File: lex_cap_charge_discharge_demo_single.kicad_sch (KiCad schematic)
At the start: 12 parts, among them J1 +5V, J2 GND, SW1 charge, SW2 discharge

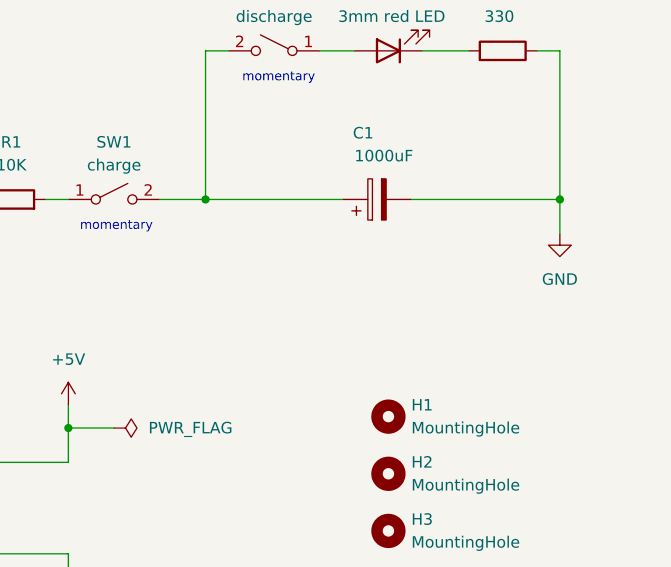
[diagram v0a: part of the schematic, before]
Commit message: Add optional component (with header) around cap
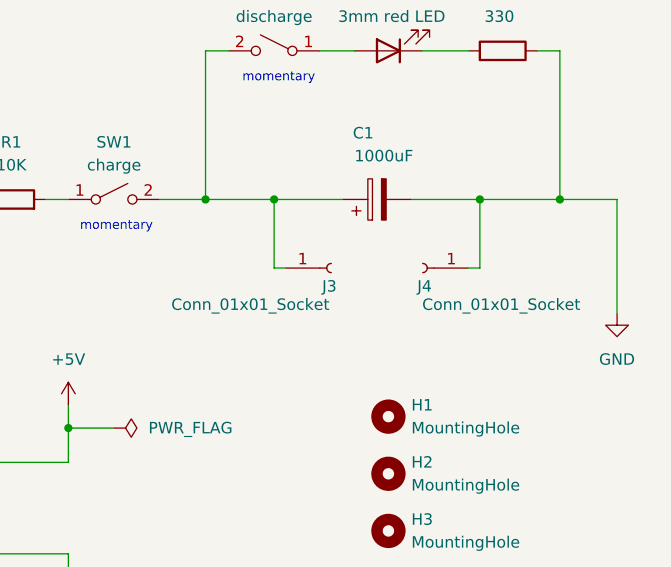
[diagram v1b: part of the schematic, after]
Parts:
- added J3, J4: Conn_01x01_Socket, Connector_PinSocket_2.54mm:PinSocket_1x01_P2.54mm_Vertical, symbol Connector:Conn_01x01_Socket
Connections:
- net GND: now also J4.1 (Pin_1)
- net at C1.1, SW1.2 (B), SW2.2 (B): now also J3.1 (Pin_1)
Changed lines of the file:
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@@
+	)
+	(junction
+		(at 167.64 44.45)
+		(diameter 0)
+		(color 0 0 0 0)
+	)
+	(junction
+		(at 144.78 44.45)
+		(diameter 0)
+		(color 0 0 0 0)
 	)
 	(junction
@@
 	(wire
 		(pts
-			(xy 160.02 44.45) (xy 176.53 44.45)
+			(xy 160.02 44.45) (xy 167.64 44.45)
+		)
+		(stroke
+			(width 0)
+			(type default)
+		)
+	)
+	(wire
+		(pts
+			(xy 144.78 44.45) (xy 152.4 44.45)
+		)
+		(stroke
+			(width 0)
+			(type default)
+		)
+	)
+	(wire
+		(pts
+			(xy 167.64 44.45) (xy 167.64 52.07)
+		)
+		(stroke
+			(width 0)
+			(type default)
+		)
+	)
+	(wire
+		(pts
+			(xy 167.64 44.45) (xy 176.53 44.45)
 		)
 		(stroke
@@
 	(wire
 		(pts
-			(xy 176.53 48.26) (xy 176.53 44.45)
+			(xy 182.88 44.45) (xy 176.53 44.45)
+		)
+		(stroke
+			(width 0)
+			(type default)
+		)
+	)
+	(wire
+		(pts
+			(xy 182.88 57.15) (xy 182.88 44.45)
+		)
+		(stroke
+			(width 0)
+			(type default)
+		)
+	)
+	(wire
+		(pts
+			(xy 144.78 52.07) (xy 146.05 52.07)
 		)
 		(stroke
@@
 	(wire
 		(pts
-			(xy 137.16 44.45) (xy 152.4 44.45)
+			(xy 144.78 44.45) (xy 144.78 52.07)
+		)
+		(stroke
+			(width 0)
+			(type default)
+		)
+	)
+	(wire
+		(pts
+			(xy 167.64 52.07) (xy 166.37 52.07)
+		)
+		(stroke
+			(width 0)
+			(type default)
+		)
+	)
+	(wire
+		(pts
+			(xy 137.16 44.45) (xy 144.78 44.45)
 		)
 		(stroke
@@
 	)
 	(symbol
+		(lib_id "Connector:Conn_01x01_Socket")
+		(at 151.13 52.07 0)
+		(unit 1)
+		(exclude_from_sim no)
+		(in_bom yes)
+		(on_board yes)
+		(dnp no)
+		(property "Reference" "J3"
+			(at 150.114 54.102 0)
+			(effects
+				(font
+					(size 1.27 1.27)
+				)
+				(justify left)
+			)
+		)
+		(property "Value" "Conn_01x01_Socket"
+			(at 133.35 56.134 0)
+			(effects
+				(font
+					(size 1.27 1.27)
+				)
+				(justify left)
+			)
+		)
+		(property "Footprint" "Connector_PinSocket_2.54mm:PinSocket_1x01_P2.54mm_Vertical"
+			(at 151.13 52.07 0)
+			(effects
+				(font
+					(size 1.27 1.27)
+				)
+				(hide yes)
+			)
+		)
+		(property "Datasheet" "~"
+			(at 151.13 52.07 0)
+			(effects
+				(font
+					(size 1.27 1.27)
+				)
+				(hide yes)
+			)
+		)
+		(property "Description" "Generic connector, single row, 01x01, script generated"
+			(at 151.13 52.07 0)
+			(effects
+				(font
+					(size 1.27 1.27)
+				)
+				(hide yes)
+			)
+		)
+		(property "Var" "Optional_Fitted Yes(+!) No(-!)"
+			(at 151.13 52.07 0)
+			(effects
+				(font
+					(size 1.27 1.27)
+				)
+				(hide yes)
+			)
+		)
+		(pin "1"
+		)
+		(instances
+			(project ""
+				(path "/4806787d-5dd8-494c-9bb0-c182769ed172"
+					(reference "J3")
+					(unit 1)
+				)
+			)
+		)
+	)
+	(symbol
+		(lib_id "Connector:Conn_01x01_Socket")
+		(at 161.29 52.07 0)
+		(mirror y)
+		(unit 1)
+		(exclude_from_sim no)
+		(in_bom yes)
+		(on_board yes)
+		(dnp no)
+		(property "Reference" "J4"
+			(at 162.306 54.102 0)
+			(effects
+				(font
+					(size 1.27 1.27)
+				)
+				(justify left)
+			)
+		)
+		(property "Value" "Conn_01x01_Socket"
+			(at 178.816 56.134 0)
+			(effects
+				(font
+					(size 1.27 1.27)
+				)
+				(justify left)
+			)
+		)
+		(property "Footprint" "Connector_PinSocket_2.54mm:PinSocket_1x01_P2.54mm_Vertical"
+			(at 161.29 52.07 0)
+			(effects
+				(font
+					(size 1.27 1.27)
+				)
+				(hide yes)
+			)
+		)
+		(property "Datasheet" "~"
+			(at 161.29 52.07 0)
+			(effects
+				(font
+					(size 1.27 1.27)
+				)
+				(hide yes)
+			)
+		)
+		(property "Description" "Generic connector, single row, 01x01, script generated"
+			(at 161.29 52.07 0)
+			(effects
+				(font
+					(size 1.27 1.27)
+				)
+				(hide yes)
+			)
+		)
+		(property "Var" "Optional_Fitted Yes(+!) No(-!)"
+			(at 161.29 52.07 0)
+			(effects
+				(font
+					(size 1.27 1.27)
+				)
+				(hide yes)
+			)
+		)
+		(pin "1"
+		)
+		(instances
+			(project "lex_cap_charge_discharge_demo_single"
+				(path "/4806787d-5dd8-494c-9bb0-c182769ed172"
+					(reference "J4")
+					(unit 1)
+				)
+			)
+		)
+	)
+	(symbol
 		(lib_id "Device:R")
 		(at 170.18 27.94 270)
@@
 	(symbol
 		(lib_id "power:GND")
-		(at 176.53 48.26 0)
+		(at 182.88 57.15 0)
 		(unit 1)
 		(exclude_from_sim no)
@@
 		(fields_autoplaced yes)
 		(property "Reference" "#PWR06"
-			(at 176.53 54.61 0)
+			(at 182.88 63.5 0)
 			(effects
 				(font
@@
 		)
 		(property "Value" "GND"
-			(at 176.53 53.34 0)
+			(at 182.88 62.23 0)
 			(effects
 				(font
@@
 		)
 		(property "Footprint" ""
-			(at 176.53 48.26 0)
+			(at 182.88 57.15 0)
 			(effects
 				(font
@@
 		)
 		(property "Datasheet" ""
-			(at 176.53 48.26 0)
+			(at 182.88 57.15 0)
 			(effects
 				(font
@@
 		)
 		(property "Description" "Power symbol creates a global label with name \"GND\" , ground"
-			(at 176.53 48.26 0)
-			(effects
-				(font
+			(at 182.88 57.15 0)
+			(effects
+				(font

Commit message: Make board bigger (4cm x 4cm), fix SMD cap to THT
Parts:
- C1: footprint Capacitor_SMD:CP_Elec_3x5.3 -> Capacitor_THT:CP_Radial_D10.0mm_P5.00mm
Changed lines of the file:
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@@
 			)
 		)
-		(property "Footprint" "Capacitor_SMD:CP_Elec_3x5.3"
+		(property "Footprint" "Capacitor_THT:CP_Radial_D10.0mm_P5.00mm"
 			(at 160.02 43.4848 0)
 			(effects

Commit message: add hunsley.io top of front, make optional headers closer to cap
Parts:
- J1, J2: footprint TestPoint:TestPoint_THTPad_2.0x2.0mm_Drill1.0mm -> TestPoint:TestPoint_THTPad_2.5x2.5mm_Drill1.2mm
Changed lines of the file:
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@@
 			)
 		)
-		(property "Footprint" "TestPoint:TestPoint_THTPad_2.0x2.0mm_Drill1.0mm"
+		(property "Footprint" "TestPoint:TestPoint_THTPad_2.5x2.5mm_Drill1.2mm"
 			(at 107.95 73.66 0)
 			(effects
@@
 			)
 		)
-		(property "Footprint" "TestPoint:TestPoint_THTPad_2.0x2.0mm_Drill1.0mm"
+		(property "Footprint" "TestPoint:TestPoint_THTPad_2.5x2.5mm_Drill1.2mm"
 			(at 107.95 83.82 0)
 			(effects
